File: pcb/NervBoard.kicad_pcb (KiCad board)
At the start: 2 copper layers, 40.6 x 87 mm, 38 parts, among them J1 Conn_01x08_Pin, J2 Conn_01x08_Pin, Q0 2N7000, Q2 2N7000, Q3 AO3400A, U1 ESP32-CAM, U2 LM1085-5.0

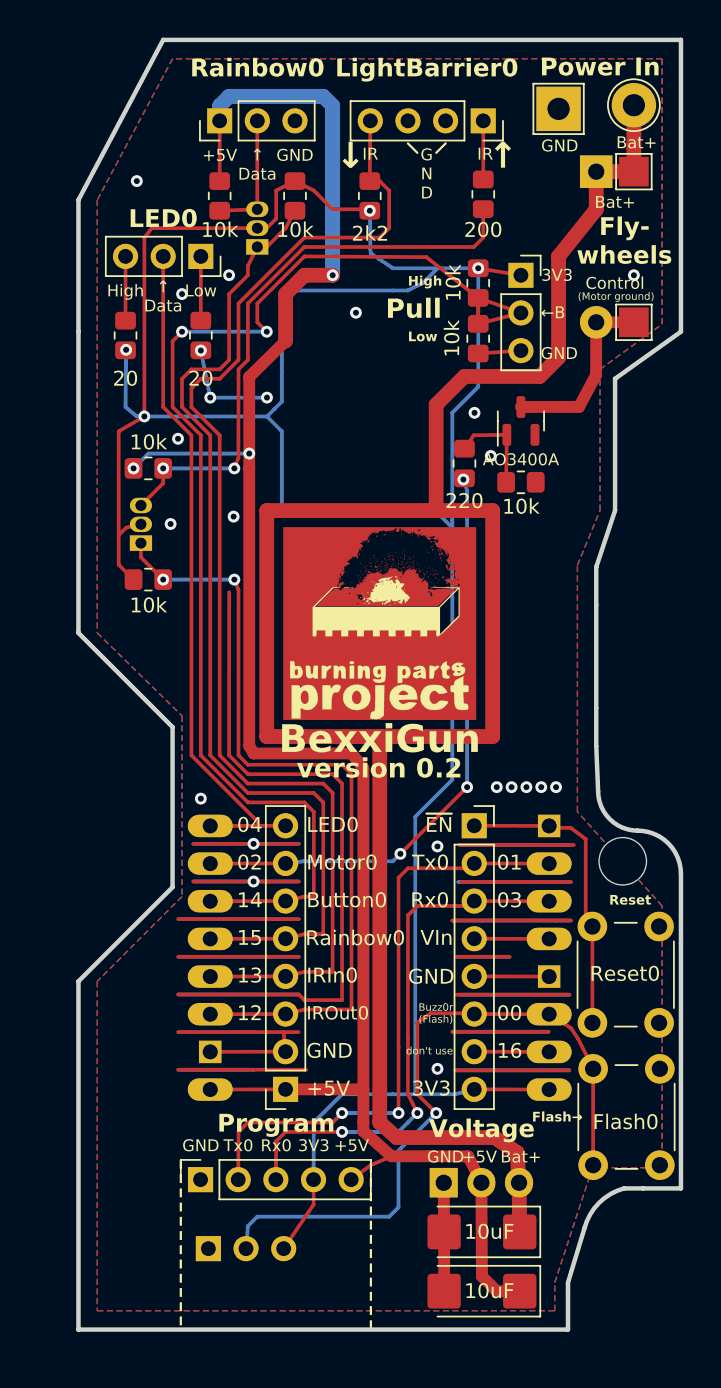
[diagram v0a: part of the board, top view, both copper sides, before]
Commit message: Added improved version of pcb v0.2 with full rewiring, focus on a more stable ground and broader wires.
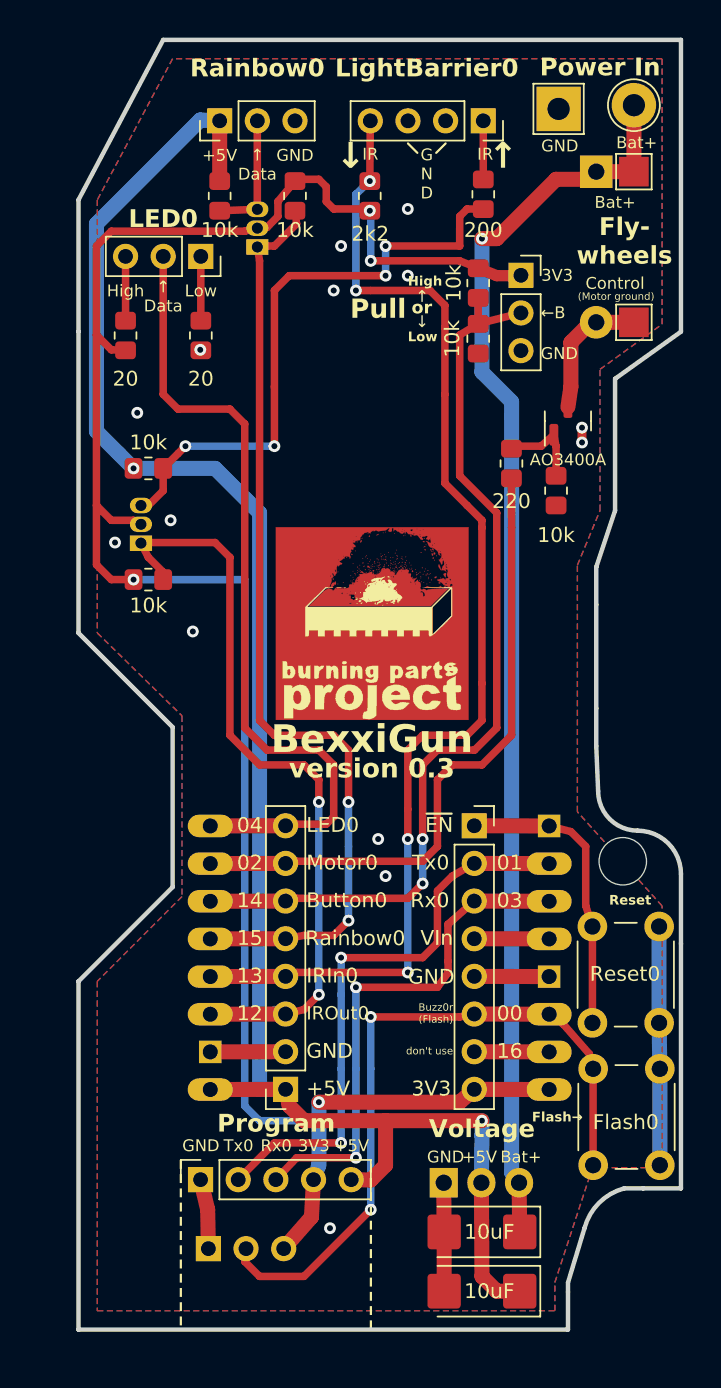
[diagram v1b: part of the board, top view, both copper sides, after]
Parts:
- moved Q3 3.17 mm to (90.8, 87.3)
- moved R_Filter_Motor0 3.17 mm to (87.0, 90.2)
- moved R_Down_Motor1 2.44 mm to (90.0, 92.0), turned to -90 degrees
- moved G*** 0.51 mm to (77.6, 101.0)
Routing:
- net GND: track 252.1 -> 38.3 mm, vias 23 -> 14
- net Bat+: track 138.3 -> 84.6 mm, vias 0 -> 1
- net 3V3: track 194.9 -> 141.2 mm
- net Button0: track 84.4 -> 62.5 mm
- net (no net): track 21.8 -> 0.00 mm
- net +5V: track 134.2 -> 122.0 mm, vias 3 -> 2
- net LED0: track 46.1 -> 55.2 mm
- net Net-(D2-A): track 12.5 -> 9.12 mm
- net DOut_3v3_0: track 67.4 -> 64.2 mm, vias 0 -> 2
- net Motor0: track 41.0 -> 43.8 mm, vias 3 -> 0
- net U0Tx: track 40.9 -> 39.1 mm
- net GPIO_IROut_0: track 39.0 -> 40.7 mm, vias 2 -> 4
- net GPIO_IROut_3v3_0: track 53.4 -> 51.7 mm
- net U0Rx: track 36.3 -> 34.9 mm
- net GPIO_IRIn_0: track 82.8 -> 81.5 mm, vias 0 -> 4
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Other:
- board text added: "version 0.3"
- board text removed: "version 0.2"

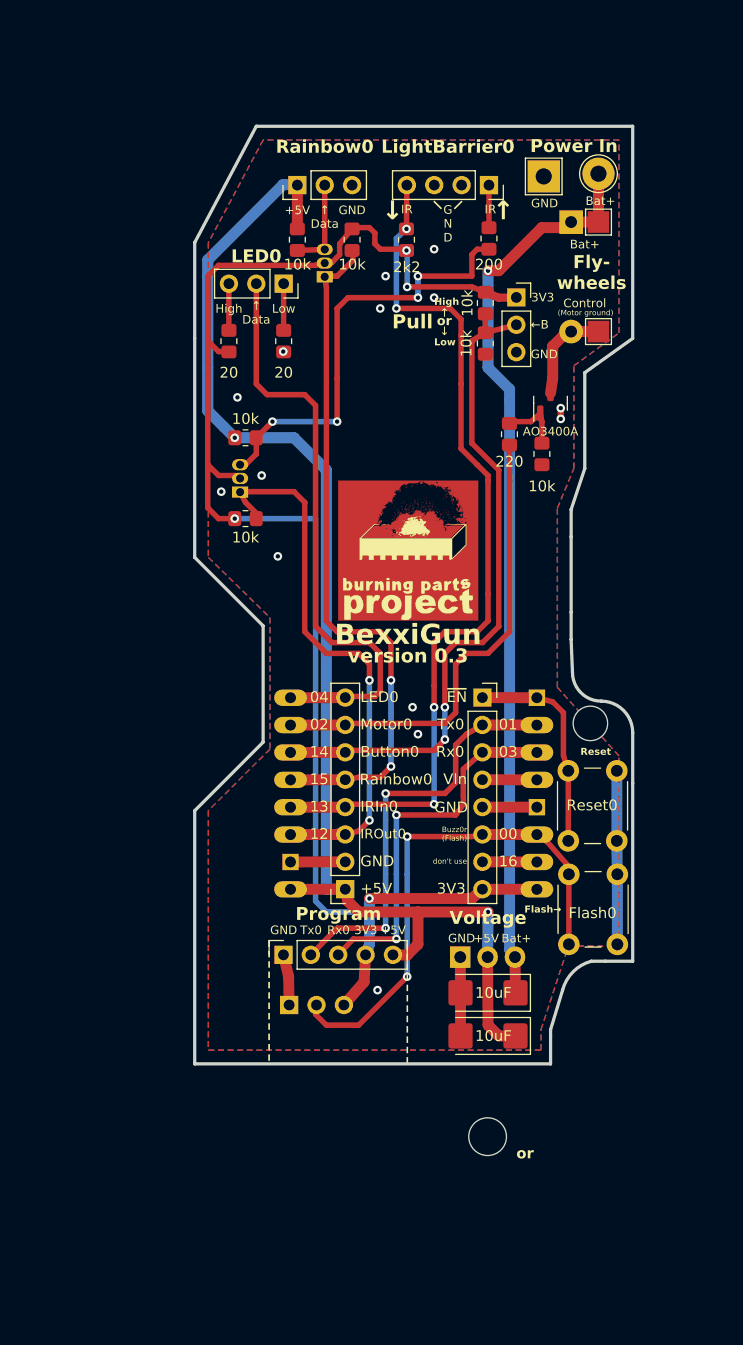
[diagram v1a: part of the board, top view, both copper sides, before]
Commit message: Improved board to a stable version
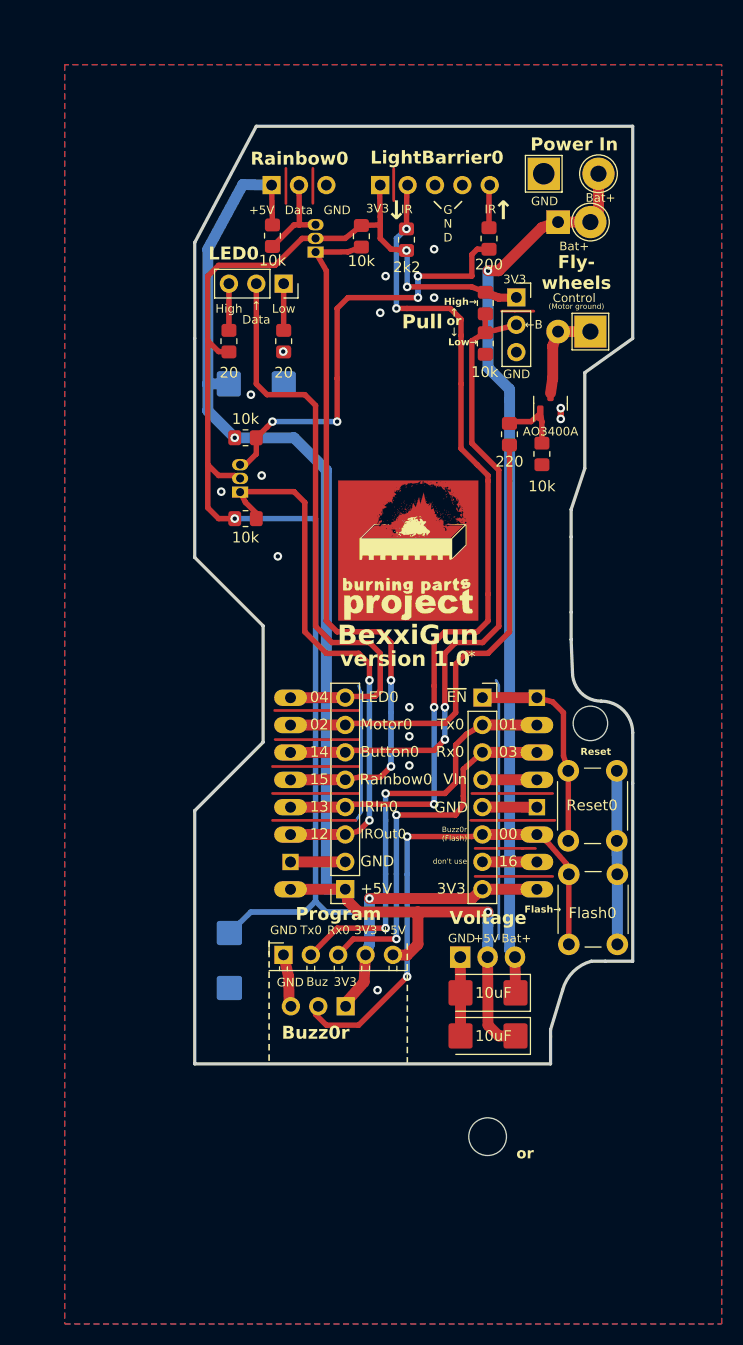
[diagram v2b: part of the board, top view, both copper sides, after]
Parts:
- added C3: 10uF, Capacitor_Tantalum_SMD:CP_EIA-6032-15_Kemet-U_Pad2.25x2.35mm_HandSolder, B.Cu at (61.0, 139.0)
- added C4: 10uF, Capacitor_Tantalum_SMD:CP_EIA-6032-15_Kemet-U_Pad2.25x2.35mm_HandSolder, B.Cu at (63.5, 85.5)
- added H4: MountingHole, PhilsLibs:MountingHole__Langloch_3.2mm_M3, F.Cu at (77.3, 85.5)
- Flywheels_Neg0: footprint TestPoint:TestPoint_Pad_2.0x2.0mm -> TestPoint:TestPoint_THTPad_3.0x3.0mm_Drill1.5mm
- Flywheels_Pos0: footprint TestPoint:TestPoint_Pad_2.0x2.0mm -> TestPoint:TestPoint_THTPad_D3.0mm_Drill1.5mm
- J_Buzzor_0: footprint Connector_PinSocket_2.54mm:PinSocket_1x03_P2.54mm_Vertical -> PhilsLibs:PinSocket_1x03_P2.54mm_Horizontal_NoPrint
- J_Prog0: footprint Connector_PinSocket_2.54mm:PinSocket_1x05_P2.54mm_Vertical -> PhilsLibs:PinSocket_1x05_P2.54mm_Horizontal_NoPrint
- LightBarrier0: value Conn_01x04_Socket -> Conn_01x05_Socket; footprint Connector_PinSocket_2.54mm:PinSocket_1x04_P2.54mm_Vertical -> PhilsLibs:PinSocket_1x05_P2.54mm_Horizontal_NoPrint; moved to B.Cu
- Rainbow0: footprint Connector_PinHeader_2.54mm:PinHeader_1x03_P2.54mm_Vertical -> PhilsLibs:PinSocket_1x03_P2.54mm_Horizontal_NoPrint; moved to B.Cu
- moved LightBarrier0 10.1 mm to (75.0, 67.1)
- moved J_Buzzor_0 5.24 mm to (71.8, 143.2), turned to 90 degrees
- moved Q0 2.45 mm to (69.0, 73.3)
- moved Rainbow0 2.39 mm to (64.9, 67.1), turned to -90 degrees
- moved R_Lvl_50 2.34 mm to (65.0, 71.8)
- moved H3 2.09 mm to (77.3, 85.5), turned to 135 degrees
- moved D2 1.21 mm to (91.5, 70.5)
- moved R_Lvl_30 0.92 mm to (73.2, 71.8)
- moved Flywheels_Neg0 0.75 mm to (94.5, 80.6)
- moved Flywheels_Pos0 0.75 mm to (94.5, 70.5)
- moved TP_Bat-1 0.25 mm to (90.2, 66.0)
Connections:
- J_Buzzor_0 pad 1: GND -> 3V3
- J_Buzzor_0 pad 3: 3V3 -> GND
- LightBarrier0 pad 1: Net-(LightBarrier0-Pin_1) -> 3V3
- LightBarrier0 pad 2: GND -> GPIO_IRIn_0
- LightBarrier0 pad 4: GPIO_IRIn_0 -> GND
- R_IROut_0 pad 1: Net-(LightBarrier0-Pin_1) -> Net-(LightBarrier0-Pin_5)
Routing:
- net GND: track 38.3 -> 154.9 mm, vias 14 -> 15
- net 3V3: track 141.2 -> 153.8 mm
- net Net-(LightBarrier0-Pin_5): track 0.00 -> 3.95 mm
- net Net-(LightBarrier0-Pin_1): track 3.95 -> 0.00 mm
- net DOut_3v3_0: track 64.2 -> 66.9 mm
- net +5V: track 122.0 -> 122.9 mm
- net Bat+: track 84.6 -> 83.7 mm
- net GPIO_IROut_3v3_0: track 51.7 -> 50.9 mm
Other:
- board text added: "*"
- board text added: "*) Every sign has a story"
- board text added: "B→"
- board text added: "Data"
- board text added: "High→"
- board text added: "If you can read this while happily soldering your ESP32"
- board text added: "LightBarrier0"
- board text added: "Low→"
- board text added: "Manuals and source code:"
- board text added: "You are holding it wrong !"
- board text added: "https://github.com/ rerebebekkkkaaaa/BexxiGun"
- board text added: "version 1.0"
- board text removed: "version 0.3"

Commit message: Added a LICENSE to make PCB re-usable
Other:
- board text added: "This PCB is published under CERN-OHL-S"
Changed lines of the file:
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@@
     (effects (font (size 0.8 0.8) (thickness 0.15)) (justify bottom mirror))
+  )
+  (gr_text "This PCB is published under CERN-OHL-S" (at 59.1 147.8) (layer "B.SilkS")
+    (effects (font (size 0.9 0.9) (thickness 0.15)) (justify right bottom mirror))
   )
   (gr_text "*) Every sign has a story" (at 91.75 135.75) (layer "B.SilkS")
